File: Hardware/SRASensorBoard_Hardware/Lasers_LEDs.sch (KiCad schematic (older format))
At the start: 24 parts, among them Q7 BSS214NW, Q8 BSS214NW, Q9 BSS214NW

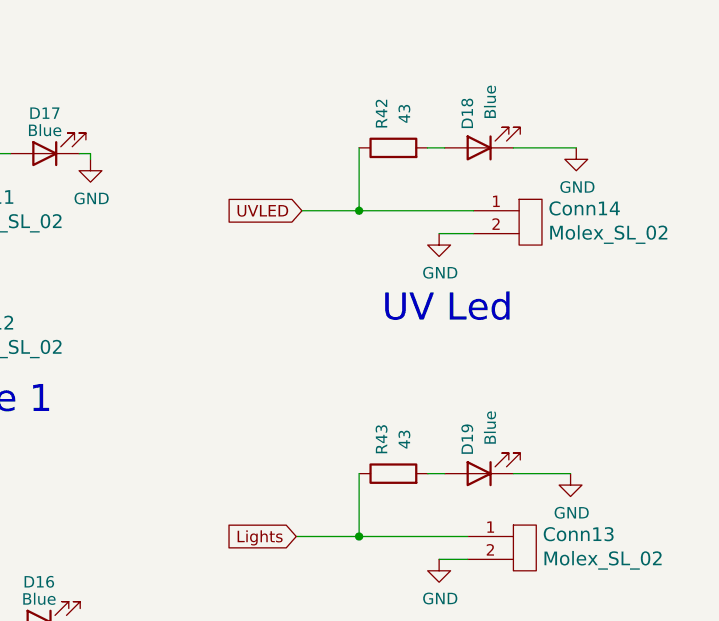
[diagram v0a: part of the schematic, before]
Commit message: changed resistor values
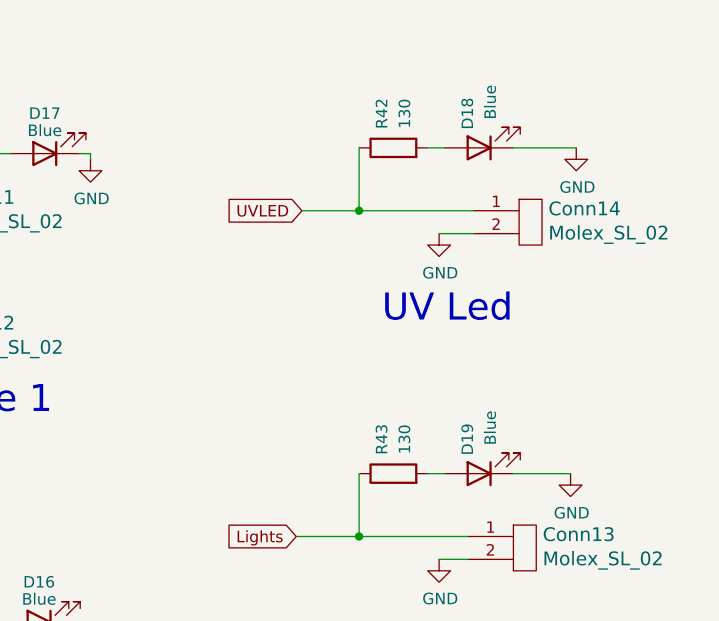
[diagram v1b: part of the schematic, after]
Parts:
- R42, R43: value 43 -> 130
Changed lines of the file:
@@
 AR Path="/61988F48/619C0986" Ref="R42"  Part="1"
 F 0 "R42" H 4625 1100 50  0000 C CNN
-F 1 "43" H 4625 1000 50  0000 C CNN
+F 1 "130" H 4625 1000 50  0000 C CNN
 F 2 "Resistor_SMD:R_0603_1608Metric_Pad1.05x0.95mm_HandSolder" V 4405 1050 50  0001 C CNN
 F 3 "~" H 4475 1050 50  0001 C CNN
@@
 AR Path="/61988F48/619C3197" Ref="R43"  Part="1"
 F 0 "R43" H 4625 2525 50  0000 C CNN
-F 1 "43" H 4625 2425 50  0000 C CNN
+F 1 "130" H 4625 2425 50  0000 C CNN
 F 2 "Resistor_SMD:R_0603_1608Metric_Pad1.05x0.95mm_HandSolder" V 4405 2475 50  0001 C CNN
 F 3 "~" H 4475 2475 50  0001 C CNN

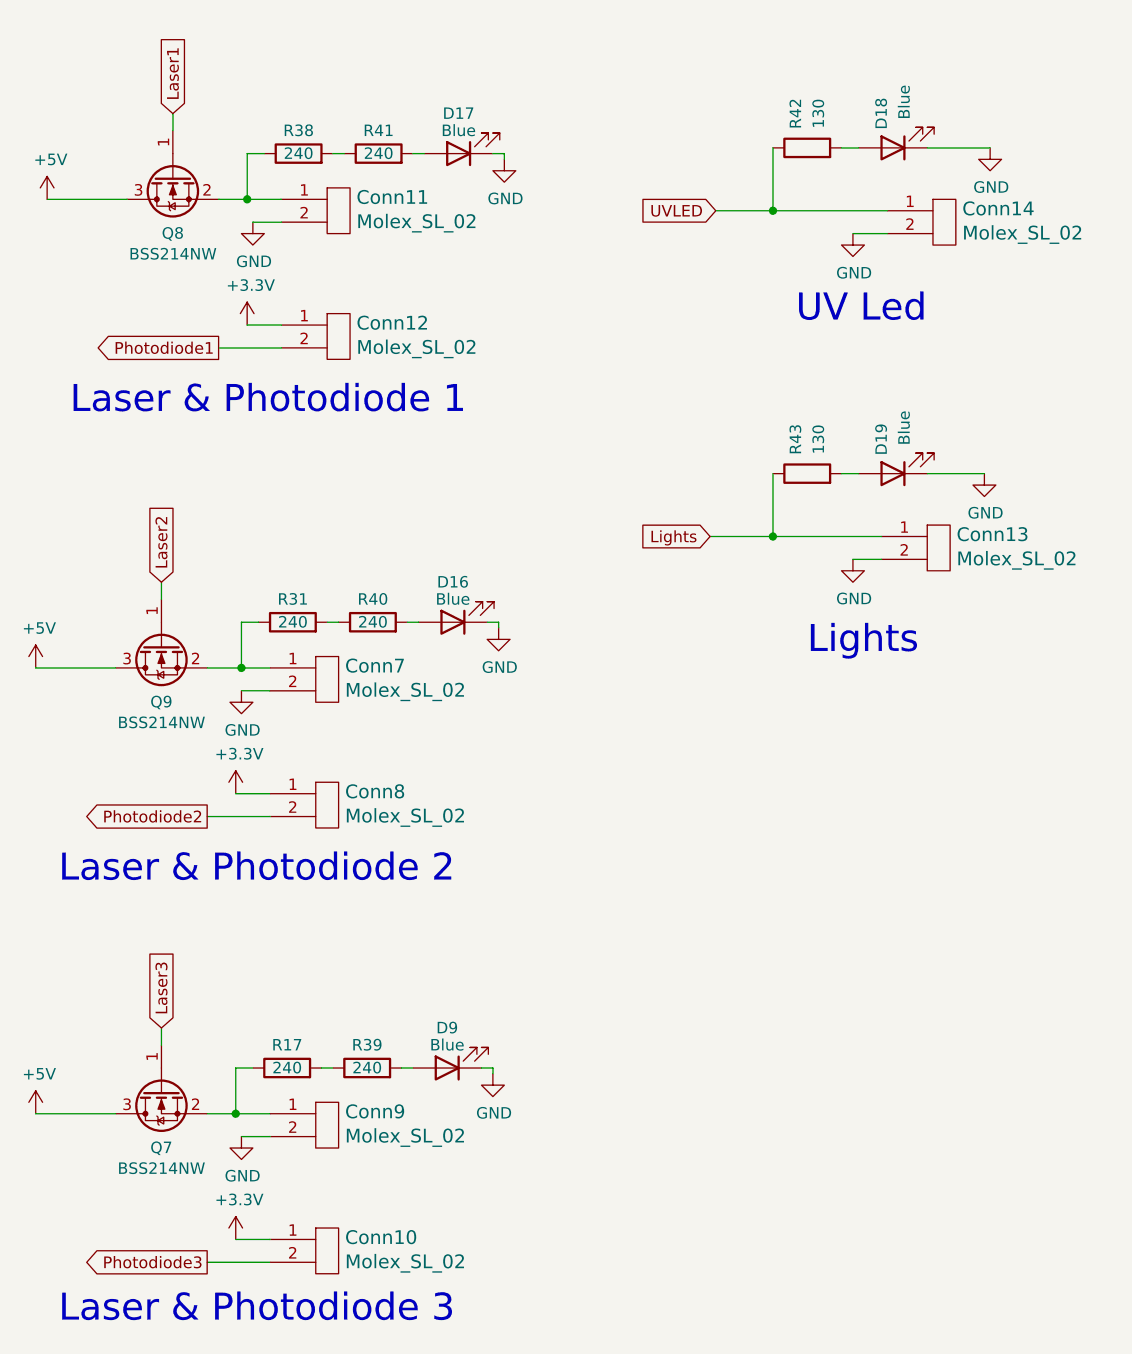
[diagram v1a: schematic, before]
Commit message: updated resistor values and moved via
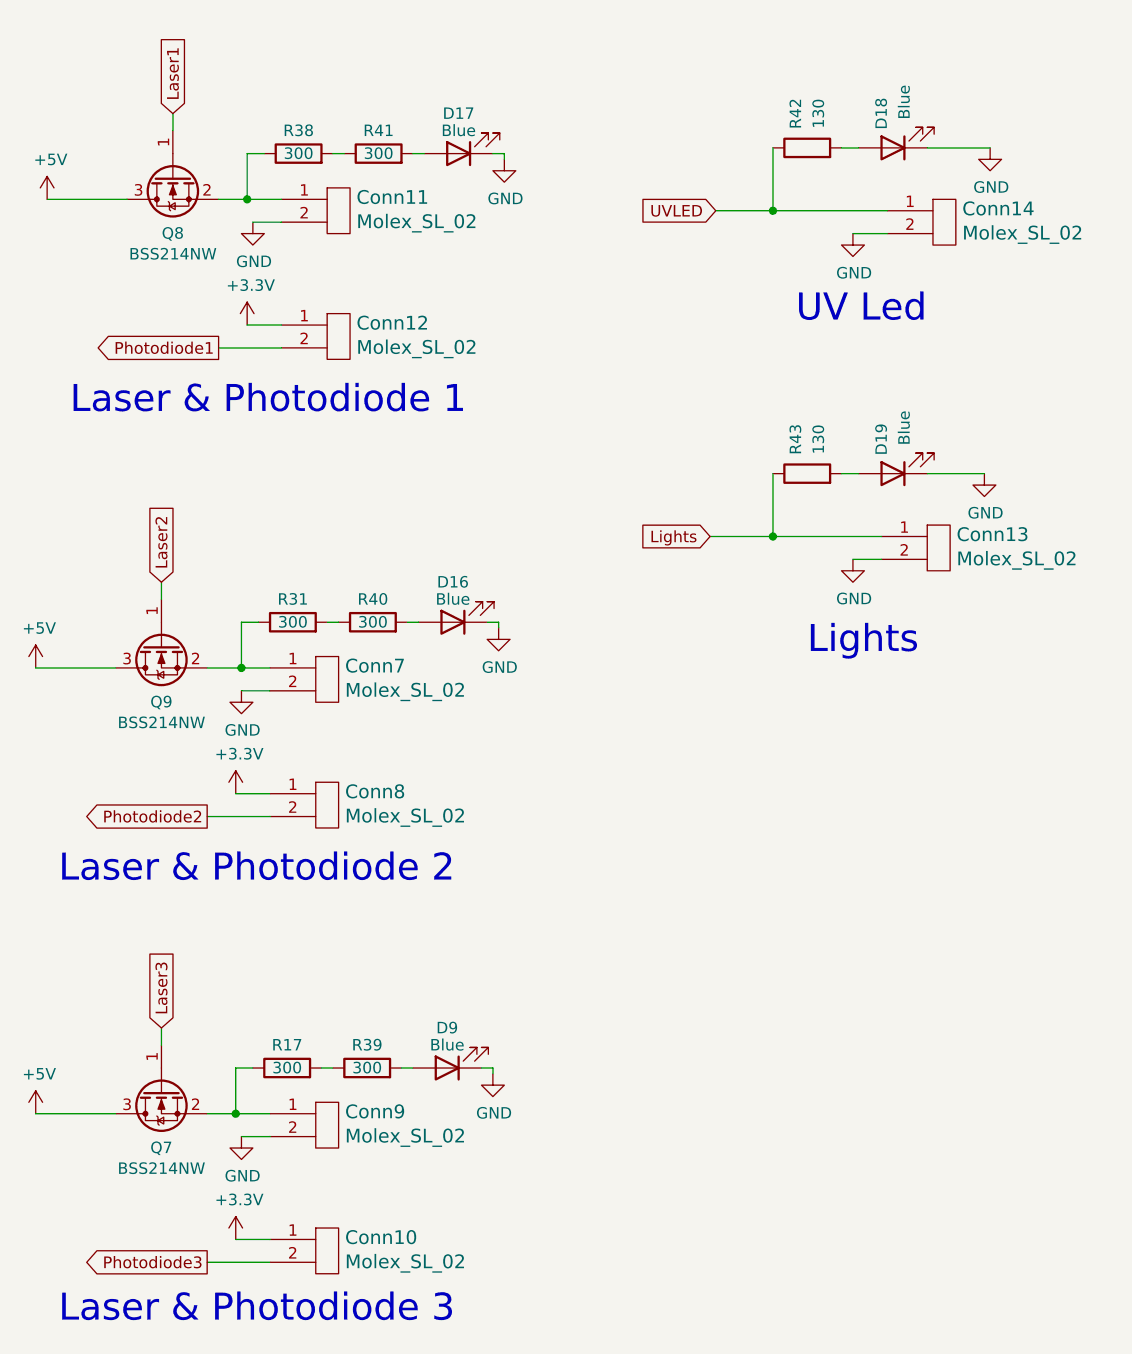
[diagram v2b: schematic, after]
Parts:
- R17, R31, R38, R39, R40, R41: value 240 -> 300
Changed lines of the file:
@@
 AR Path="/61988F48/619A3177" Ref="R38"  Part="1"
 F 0 "R38" V 2350 1075 50  0000 C CNN
-F 1 "240" V 2250 1075 50  0000 C CNN
+F 1 "300" V 2250 1075 50  0000 C CNN
 F 2 "Resistor_SMD:R_0603_1608Metric_Pad1.05x0.95mm_HandSolder" V 2180 1075 50  0001 C CNN
 F 3 "~" H 2250 1075 50  0001 C CNN
@@
 AR Path="/61988F48/619A318C" Ref="R41"  Part="1"
 F 0 "R41" V 2700 1075 50  0000 C CNN
-F 1 "240" V 2600 1075 50  0000 C CNN
+F 1 "300" V 2600 1075 50  0000 C CNN
 F 2 "Resistor_SMD:R_0603_1608Metric_Pad1.05x0.95mm_HandSolder" V 2530 1075 50  0001 C CNN
 F 3 "~" H 2600 1075 50  0001 C CNN
@@
 AR Path="/61988F48/619A7FF7" Ref="R31"  Part="1"
 F 0 "R31" V 2325 3125 50  0000 C CNN
-F 1 "240" V 2225 3125 50  0000 C CNN
+F 1 "300" V 2225 3125 50  0000 C CNN
 F 2 "Resistor_SMD:R_0603_1608Metric_Pad1.05x0.95mm_HandSolder" V 2155 3125 50  0001 C CNN
 F 3 "~" H 2225 3125 50  0001 C CNN
@@
 AR Path="/61988F48/619A800C" Ref="R40"  Part="1"
 F 0 "R40" V 2675 3125 50  0000 C CNN
-F 1 "240" V 2575 3125 50  0000 C CNN
+F 1 "300" V 2575 3125 50  0000 C CNN
 F 2 "Resistor_SMD:R_0603_1608Metric_Pad1.05x0.95mm_HandSolder" V 2505 3125 50  0001 C CNN
 F 3 "~" H 2575 3125 50  0001 C CNN
@@
 AR Path="/61988F48/619AC625" Ref="R17"  Part="1"
 F 0 "R17" V 2300 5075 50  0000 C CNN
-F 1 "240" V 2200 5075 50  0000 C CNN
+F 1 "300" V 2200 5075 50  0000 C CNN
 F 2 "Resistor_SMD:R_0603_1608Metric_Pad1.05x0.95mm_HandSolder" V 2130 5075 50  0001 C CNN
 F 3 "~" H 2200 5075 50  0001 C CNN
@@
 AR Path="/61988F48/619AC63A" Ref="R39"  Part="1"
 F 0 "R39" V 2650 5075 50  0000 C CNN
-F 1 "240" V 2550 5075 50  0000 C CNN
+F 1 "300" V 2550 5075 50  0000 C CNN
 F 2 "Resistor_SMD:R_0603_1608Metric_Pad1.05x0.95mm_HandSolder" V 2480 5075 50  0001 C CNN
 F 3 "~" H 2550 5075 50  0001 C CNN

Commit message: added board mounts and did rev 2 changes
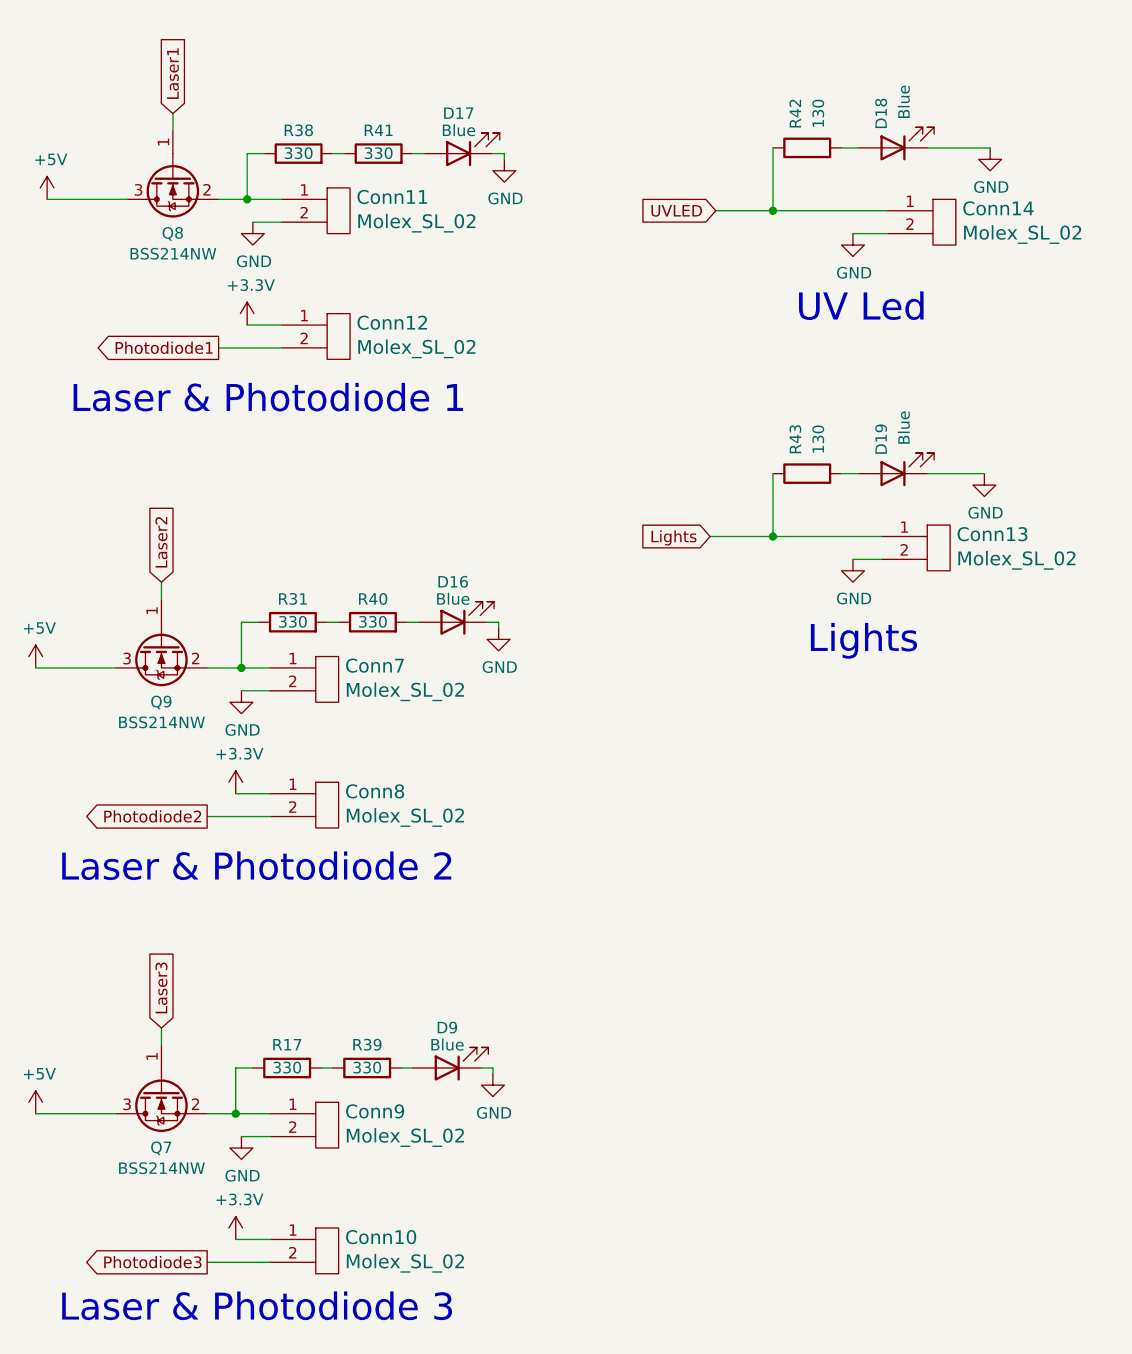
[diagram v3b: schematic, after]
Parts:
- R17, R31, R38, R39, R40, R41: value 300 -> 330; footprint Resistor_SMD:R_0603_1608Metric_Pad1.05x0.95mm_HandSolder -> Resistor_SMD:R_0603_1608Metric_Pad0.98x0.95mm_HandSolder
- R42, R43: footprint Resistor_SMD:R_0603_1608Metric_Pad1.05x0.95mm_HandSolder -> Resistor_SMD:R_0603_1608Metric_Pad0.98x0.95mm_HandSolder
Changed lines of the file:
@@
 AR Path="/61988F48/619A3177" Ref="R38"  Part="1"
 F 0 "R38" V 2350 1075 50  0000 C CNN
-F 1 "300" V 2250 1075 50  0000 C CNN
-F 2 "Resistor_SMD:R_0603_1608Metric_Pad1.05x0.95mm_HandSolder" V 2180 1075 50  0001 C CNN
+F 1 "330" V 2250 1075 50  0000 C CNN
+F 2 "Resistor_SMD:R_0603_1608Metric_Pad0.98x0.95mm_HandSolder" V 2180 1075 50  0001 C CNN
 F 3 "~" H 2250 1075 50  0001 C CNN
 	1    2250 1075
@@
 AR Path="/61988F48/619A318C" Ref="R41"  Part="1"
 F 0 "R41" V 2700 1075 50  0000 C CNN
-F 1 "300" V 2600 1075 50  0000 C CNN
-F 2 "Resistor_SMD:R_0603_1608Metric_Pad1.05x0.95mm_HandSolder" V 2530 1075 50  0001 C CNN
+F 1 "330" V 2600 1075 50  0000 C CNN
+F 2 "Resistor_SMD:R_0603_1608Metric_Pad0.98x0.95mm_HandSolder" V 2530 1075 50  0001 C CNN
 F 3 "~" H 2600 1075 50  0001 C CNN
 	1    2600 1075
@@
 AR Path="/61988F48/619A7FF7" Ref="R31"  Part="1"
 F 0 "R31" V 2325 3125 50  0000 C CNN
-F 1 "300" V 2225 3125 50  0000 C CNN
-F 2 "Resistor_SMD:R_0603_1608Metric_Pad1.05x0.95mm_HandSolder" V 2155 3125 50  0001 C CNN
+F 1 "330" V 2225 3125 50  0000 C CNN
+F 2 "Resistor_SMD:R_0603_1608Metric_Pad0.98x0.95mm_HandSolder" V 2155 3125 50  0001 C CNN
 F 3 "~" H 2225 3125 50  0001 C CNN
 	1    2225 3125
@@
 AR Path="/61988F48/619A800C" Ref="R40"  Part="1"
 F 0 "R40" V 2675 3125 50  0000 C CNN
-F 1 "300" V 2575 3125 50  0000 C CNN
-F 2 "Resistor_SMD:R_0603_1608Metric_Pad1.05x0.95mm_HandSolder" V 2505 3125 50  0001 C CNN
+F 1 "330" V 2575 3125 50  0000 C CNN
+F 2 "Resistor_SMD:R_0603_1608Metric_Pad0.98x0.95mm_HandSolder" V 2505 3125 50  0001 C CNN
 F 3 "~" H 2575 3125 50  0001 C CNN
 	1    2575 3125
@@
 AR Path="/61988F48/619AC625" Ref="R17"  Part="1"
 F 0 "R17" V 2300 5075 50  0000 C CNN
-F 1 "300" V 2200 5075 50  0000 C CNN
-F 2 "Resistor_SMD:R_0603_1608Metric_Pad1.05x0.95mm_HandSolder" V 2130 5075 50  0001 C CNN
+F 1 "330" V 2200 5075 50  0000 C CNN
+F 2 "Resistor_SMD:R_0603_1608Metric_Pad0.98x0.95mm_HandSolder" V 2130 5075 50  0001 C CNN
 F 3 "~" H 2200 5075 50  0001 C CNN
 	1    2200 5075
@@
 AR Path="/61988F48/619AC63A" Ref="R39"  Part="1"
 F 0 "R39" V 2650 5075 50  0000 C CNN
-F 1 "300" V 2550 5075 50  0000 C CNN
-F 2 "Resistor_SMD:R_0603_1608Metric_Pad1.05x0.95mm_HandSolder" V 2480 5075 50  0001 C CNN
+F 1 "330" V 2550 5075 50  0000 C CNN
+F 2 "Resistor_SMD:R_0603_1608Metric_Pad0.98x0.95mm_HandSolder" V 2480 5075 50  0001 C CNN
 F 3 "~" H 2550 5075 50  0001 C CNN
 	1    2550 5075
@@
 F 0 "R42" H 4625 1100 50  0000 C CNN
 F 1 "130" H 4625 1000 50  0000 C CNN
-F 2 "Resistor_SMD:R_0603_1608Metric_Pad1.05x0.95mm_HandSolder" V 4405 1050 50  0001 C CNN
+F 2 "Resistor_SMD:R_0603_1608Metric_Pad0.98x0.95mm_HandSolder" V 4405 1050 50  0001 C CNN
 F 3 "~" H 4475 1050 50  0001 C CNN
 	1    4475 1050
@@
 F 0 "R43" H 4625 2525 50  0000 C CNN
 F 1 "130" H 4625 2425 50  0000 C CNN
-F 2 "Resistor_SMD:R_0603_1608Metric_Pad1.05x0.95mm_HandSolder" V 4405 2475 50  0001 C CNN
+F 2 "Resistor_SMD:R_0603_1608Metric_Pad0.98x0.95mm_HandSolder" V 4405 2475 50  0001 C CNN
 F 3 "~" H 4475 2475 50  0001 C CNN
 	1    4475 2475
